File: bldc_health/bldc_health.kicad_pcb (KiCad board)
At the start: 2 copper layers, 30.1 x 30.1 mm, 51 parts, among them J1 USB-C, J2 UART, J6 SWD, SW1 BOOT_SW, SW2 RESET_SW, U1 STM32G491, U2 ASM330, U3 ICM40609, U4 AMS1117-3.3, Y1 HSE 8MHz

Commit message: changes to pins
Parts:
- C1, C10, C11, C12, C13, C14, C16, C17, C18, C19, C2, C20, C3, C4, C5, C6, C7, C8, C9: footprint C_0603_1608Metric_Pad1.08x0.95mm_HandSolder -> Capacitor_SMD:C_0603_1608Metric_Pad1.08x0.95mm_HandSolder
- C15: value 10n -> 10N; footprint C_0603_1608Metric_Pad1.08x0.95mm_HandSolder -> Capacitor_SMD:C_0603_1608Metric_Pad1.08x0.95mm_HandSolder
- D2: footprint LED_0805_2012Metric_Pad1.15x1.40mm_HandSolder -> LED_SMD:LED_0805_2012Metric_Pad1.15x1.40mm_HandSolder
- D4: value DEBUG LED -> debug_led; footprint LED_0805_2012Metric_Pad1.15x1.40mm_HandSolder -> LED_SMD:LED_0805_2012Metric_Pad1.15x1.40mm_HandSolder
- F2: value Polyfuse -> Polyfuse_Small; footprint Fuse_0603_1608Metric_Pad1.05x0.95mm_HandSolder -> Fuse:Fuse_0603_1608Metric_Pad1.05x0.95mm_HandSolder
- FB2: footprint L_0603_1608Metric_Pad1.05x0.95mm_HandSolder -> Inductor_SMD:L_0603_1608Metric_Pad1.05x0.95mm_HandSolder
- J1: value USB-C -> USB_C_Receptacle_USB2.0_14P
- J6: value SWD -> SERIAL; footprint PinHeader_1x05_P2.54mm_Vertical -> Connector_PinHeader_2.54mm:PinHeader_1x05_P2.54mm_Vertical
- JP6: value ADDR_ICM -> ICM_SJ
- JP7: value ADDR_ASM -> ICM_SJ
- R1, R10, R12, R2, R3, R4, R5, R6, R7, R8, R9: footprint R_0603_1608Metric_Pad0.98x0.95mm_HandSolder -> Resistor_SMD:R_0603_1608Metric_Pad0.98x0.95mm_HandSolder
- SW1: value BOOT_SW -> SW_SPDT; footprint SW_Slide-03_Wuerth-WS-SLTV_10x2.5x6.4_P2.54mm -> Button_Switch_THT:SW_Slide-03_Wuerth-WS-SLTV_10x2.5x6.4_P2.54mm
- SW2: value RESET_SW -> Reset
- U1: value STM32G491 -> ~; footprint QFN-48-1EP_7x7mm_P0.5mm_EP5.6x5.6mm -> EasyEDA_Lib:UFQFPN-48_L7.0-W7.0-P0.50-TL-EP5.6
- U2: value ASM330 -> ~; footprint LGA-14_3x2.5mm_P0.5mm_LayoutBorder3x4y -> EasyEDA_Lib:LGA-14_L3.0-W2.5-P0.50-TL
- U3: value ICM40609 -> ~; footprint InvenSense_QFN-24_3x3mm_P0.4mm -> EasyEDA_Lib:LGA-24_L3.0-W3.0-P0.40-TL
- U4: footprint SOT-223-3_TabPin2 -> Package_TO_SOT_SMD:SOT-223-3_TabPin2
- Y1: value HSE 8MHz -> Crystal; footprint Crystal_SMD_HC49-SD -> Crystal:Crystal_SMD_HC49-SD
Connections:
- J1 pad A1: GND -> (no net)
- J1 pad A4: /VBUS -> (no net)
- J1 pad SH: GND -> (no net)
- U1 pad 30: /SCL_ASM -> /SDA_ASM
- U1 pad 31: unconnected-(U1-PA9-Pad31) -> /SCL_ASM
- U1 pad 40: /SDA_ASM -> unconnected-(U1-PC11-Pad40)

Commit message: Update PCB layout and schematic
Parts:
- removed MH1, MH3, MH4: MountingHole_M3, MountingHole_3.2mm_M3_Pad_Via
- added MH2: MountingHole_M3, MountingHole_3.2mm_M3_Pad_Via, B.Cu at (102.9, 104.5)
- added MH5: MountingHole_M3, MountingHole_3.2mm_M3_Pad_Via, B.Cu at (126.2, 104.5)
- added MH6: MountingHole_M3, MountingHole_3.2mm_M3_Pad_Via, B.Cu at (102.9, 127.8)
- moved MH7 24.5 mm to (126.2, 127.8)
- moved FB2 7.17 mm to (130.1, 121.3), turned to -90 degrees
- moved C16 5.64 mm to (109.7, 128.7)
- moved C4 4.63 mm to (122.8, 131.7), turned to -90 degrees
- moved C17 4.13 mm to (117.2, 126.5), turned to 180 degrees
- moved Y1 3.56 mm to (113.5, 130.5)
- moved C3 3.14 mm to (130.4, 125.0)
- moved C19 2.77 mm to (121.0, 125.6)
- moved C20 2.00 mm to (121.1, 128.5), turned to -90 degrees
- moved C9 1.75 mm to (127.1, 123.3)
- moved C10 0.44 mm to (114.8, 117.9)
- moved C11 0.44 mm to (115.3, 115.1)
- moved C18 0.44 mm to (103.0, 126.9)
- moved C6 0.44 mm to (114.7, 120.5)
- moved C8 0.44 mm to (127.4, 117.0)
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- renumbered MH2 to MH7
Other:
- board size 30.1 x 30.1 mm -> 35.4 x 35.3 mm

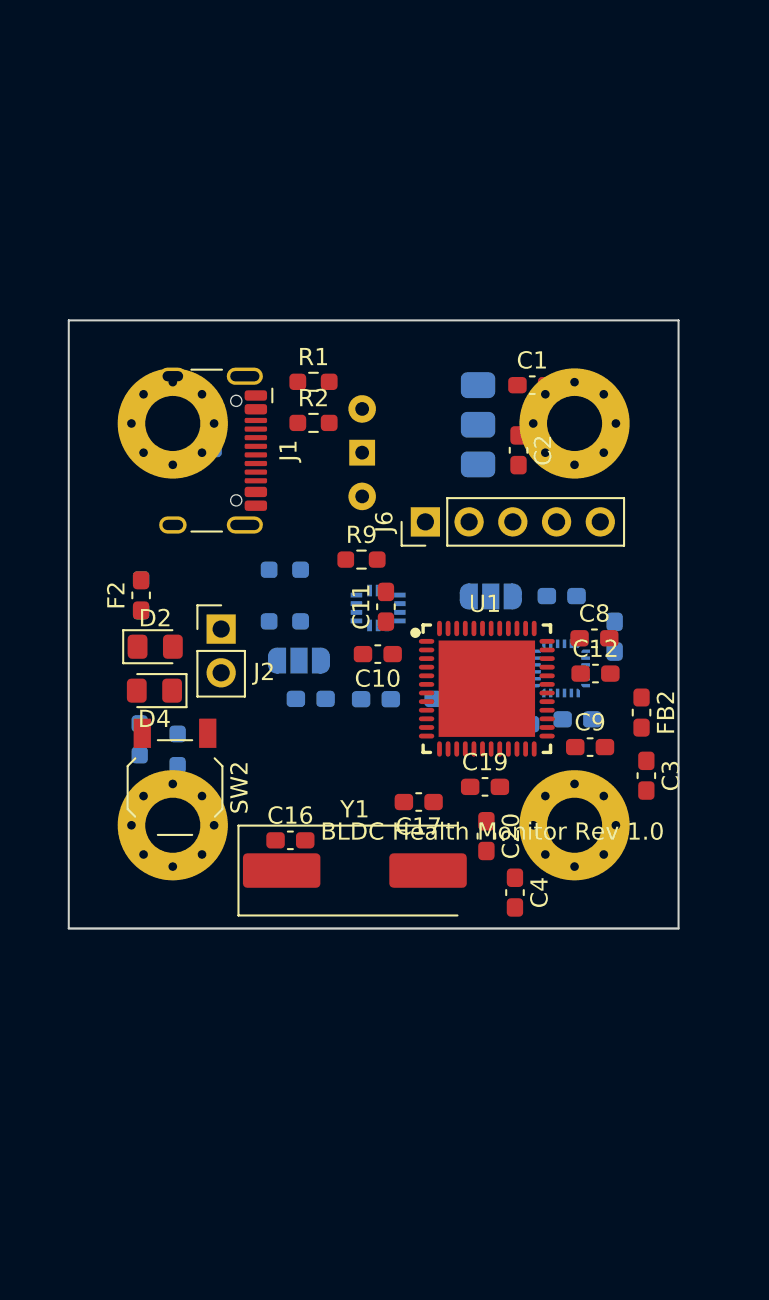
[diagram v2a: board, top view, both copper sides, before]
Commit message: Update PCB layout, footprints, and schematic
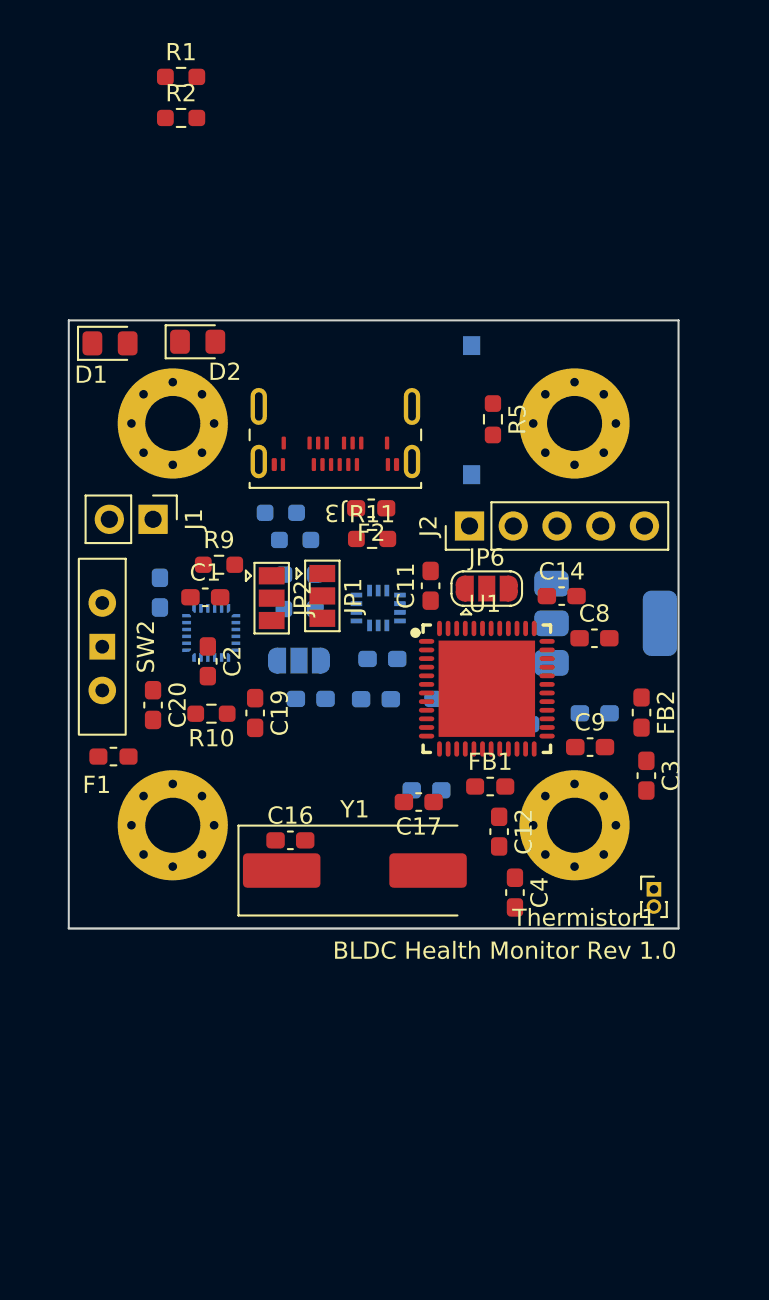
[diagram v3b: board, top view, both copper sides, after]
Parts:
- removed D4: debug_led, LED_SMD:LED_0805_2012Metric_Pad1.15x1.40mm_HandSolder
- removed J6: SERIAL, Connector_PinHeader_2.54mm:PinHeader_1x05_P2.54mm_Vertical
- added D1: 5V LED, LED_SMD:LED_0805_2012Metric_Pad1.15x1.40mm_HandSolder, F.Cu at (99.2, 99.8)
- added F1: Polyfuse_Small, Fuse:Fuse_0603_1608Metric_Pad1.05x0.95mm_HandSolder, F.Cu at (99.4, 123.8)
- added FB1: 120R, Inductor_SMD:L_0603_1608Metric_Pad1.05x0.95mm_HandSolder, F.Cu at (121.3, 125.6)
- added J3: USB_C_Receptacle_USB2.0_14P, Connector_USB:USB_C_Receptacle_Amphenol_124019772112A, F.Cu at (112.3, 103.7)
- added JP1: ICM_SJ, Jumper:SolderJumper-3_P1.3mm_Open_Pad1.0x1.5mm, F.Cu at (111.6, 114.5)
- added JP2: ICM_SJ, Jumper:SolderJumper-3_P1.3mm_Open_Pad1.0x1.5mm, F.Cu at (108.6, 114.6)
- added R11: 5k1, Resistor_SMD:R_0603_1608Metric_Pad0.98x0.95mm_HandSolder, F.Cu at (114.5, 111.2)
- added Thermistor1: 10k, Connector_PinHeader_1.00mm:PinHeader_1x02_P1.00mm_Vertical, F.Cu at (130.8, 131.6)
- C1, C2: value 10u -> 100n
- C10: value 100nF -> 100n; moved to B.Cu
- C12: value 100nF -> 10uF
- C13: value 100n -> 100nF
- C14: value 2.2u -> 100nF; moved to F.Cu
- C15: value 10N -> 100nF
- C16, C17: value 33p -> 10u
- C18: value 100nF -> 10N
- C20: value 1uF -> 2.2u
- C3: value 10uF -> 100n
- C4, C6: value 100n -> 33p
- C5: value 100n -> 10u
- C7: value 10u -> 1uF
- D2: value 5V LED -> debug_led
- J1: value USB_C_Receptacle_USB2.0_14P -> UART; footprint USB_C_Receptacle_HCTL_HC-TYPE-C-16P-01A -> Connector_PinHeader_2.54mm:PinHeader_1x02_P2.54mm_Vertical
- J2: value UART -> SERIAL; footprint PinHeader_1x02_P2.54mm_Vertical -> Connector_PinHeader_2.54mm:PinHeader_1x05_P2.54mm_Vertical
- JP6, R10: moved to F.Cu
- R1: value 5k1 -> 500
- R12: value 500 -> 5k1
- R2: value 5k1 -> 1k
- R5: value 1k5 -> 10k; moved to F.Cu
- R8: value 1k -> 1k5
- SW1: value SW_SPDT -> Reset; footprint Button_Switch_THT:SW_Slide-03_Wuerth-WS-SLTV_10x2.5x6.4_P2.54mm -> TS09-63-25-WT-160-SMT-TR:SW_TS09-63-25-WT-160-SMT-TR
- SW2: value Reset -> SW_SPDT; footprint SW_SPST_TL3342 -> Button_Switch_THT:SW_Slide-03_Wuerth-WS-SLTV_10x2.5x6.4_P2.54mm
- U3: value ~ -> AMS1117-3.3; footprint EasyEDA_Lib:LGA-24_L3.0-W3.0-P0.40-TL -> Package_TO_SOT_SMD:SOT-223-3_TabPin2
- U4: value AMS1117-3.3 -> ~; footprint Package_TO_SOT_SMD:SOT-223-3_TabPin2 -> EasyEDA_Lib:LGA-24_L3.0-W3.0-P0.40-TL
- moved C1 22.6 mm to (104.8, 114.6)
- moved U4 22.2 mm to (105.1, 116.7)
- moved C2 21.8 mm to (104.9, 118.3)
- moved C20 20.8 mm to (101.7, 120.8)
- moved R1 19.3 mm to (103.4, 84.4)
- moved R2 19.3 mm to (103.4, 86.8)
- moved D2 17.9 mm to (104.3, 99.8)
- moved R5 17.2 mm to (121.5, 104.2), turned to -90 degrees
- moved J2 15.6 mm to (120.1, 110.5), turned to 90 degrees
- moved R8 15.5 mm to (109.2, 109.7), turned to 180 degrees
- moved F2 14.3 mm to (114.4, 109.4), turned to 180 degrees
- moved C19 14.0 mm to (107.7, 121.3), turned to -90 degrees
- moved C15 13.5 mm to (115.0, 118.2), turned to 0 degrees
- moved C18 12.6 mm to (102.1, 114.3), turned to -90 degrees
- moved C12 10.8 mm to (121.8, 128.2), turned to -90 degrees
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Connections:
- C1 pad 1: /VBUS -> /VDDA
- C10 pad 1: /VDD_STM -> /VDDA
- C13 pad 1: /VDD -> /VDD_STM
- C14 pad 1: /VDD -> /VDD_STM
- C15 pad 1: GND -> /VDD_STM
- C15 pad 2: /VDD -> GND
- C16 pad 1: /HSE_IN -> /VBUS
- C17 pad 1: /HSE_OUT -> /VDD
- C18 pad 2: /Reset -> /VDD
- C19 pad 1: /VDDA -> /VDD
- C20 pad 1: /VDDA -> /VDD
- C3 pad 1: /VDD_STM -> /VDD
- C4 pad 1: /VDDA -> /HSE_IN
- C6 pad 1: /VDD -> /HSE_OUT
- C7 pad 1: /VDD -> /VDDA
- C9 pad 1: /VDD_STM -> GND
- C9 pad 2: GND -> /Reset
- D2 pad 1: Net-(D2-K) -> GND
- D2 pad 2: /VBUS -> Net-(D2-A)
- J2 pad 1: /PA2_TX -> /VDD
- J2 pad 2: /PA3_RX -> /SWDIO
- R1 pad 1: Net-(J1-CC1) -> Net-(D1-K)
- R10 pad 1: /Reset -> /SCL_ICM
- R12 pad 1: Net-(D2-K) -> Net-(J3-CC2)
- R2 pad 1: Net-(J1-CC2) -> Net-(D2-A)
- R2 pad 2: GND -> /PB2
- R5 pad 1: /USB_D+ -> /Reset
- R6 pad 1: /VDD -> /VDDA
- R6 pad 2: /SDA_ICM -> /PA0
- R7 pad 1: /SCL_ICM -> Net-(SW2-B)
- R7 pad 2: /VDD -> /Boot0
- R8 pad 1: Net-(D4-A) -> /USB_D+
- R8 pad 2: /PB2 -> /VDD
- R9 pad 1: Net-(SW1-B) -> /VDD
- R9 pad 2: /Boot0 -> /SDA_ICM
- SW1 pad 1: GND -> /Reset
- SW1 pad 2: Net-(SW1-B) -> GND
- SW2 pad 1: /Reset -> GND
- SW2 pad 2: GND -> Net-(SW2-B)
- U1 pad 8: unconnected-(U1-PA0-Pad8) -> /PA0
- U2 pad 1: Net-(JP7-C) -> Net-(JP1-C)
- U3 pad 1: unconnected-(U3-NC-Pad1) -> GND
- U3 pad 2: unconnected-(U3-NC-Pad2) -> /VDD
- U3 pad 3: unconnected-(U3-NC-Pad3) -> /VBUS
- U4 pad 1: GND -> unconnected-(U4-NC-Pad1)
- U4 pad 2: /VDD -> unconnected-(U4-NC-Pad2)
- U4 pad 3: /VBUS -> unconnected-(U4-NC-Pad3)

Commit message: Back up current PCB and design settings before routing cleanup
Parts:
- R2: moved to B.Cu
- moved R2 39.0 mm to (113.6, 124.4), turned to 90 degrees
- moved D2 26.0 mm to (110.2, 125.0)
- moved R1 20.8 mm to (97.9, 104.4), turned to -90 degrees
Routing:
- net /VDD: track 0.00 -> 133.5 mm, vias 0 -> 16
- net /VDD_STM: track 0.00 -> 115.8 mm, vias 0 -> 14
- net /INT1: track 0.00 -> 87.8 mm, vias 0 -> 7
- net /VBUS: track 0.00 -> 69.4 mm, vias 0 -> 3
- net /VDDA: track 0.00 -> 60.2 mm, vias 0 -> 2
- net /PA3_RX: track 0.00 -> 48.8 mm, vias 0 -> 4
- net Net-(SW2-B): track 0.00 -> 46.4 mm, vias 0 -> 1
- net /Reset: track 0.00 -> 44.6 mm, vias 0 -> 1
- net /PB0_INT1_ICM: track 0.00 -> 32.5 mm, vias 0 -> 4
- net /PA0: track 0.00 -> 17.5 mm
- net /SWDIO: track 0.00 -> 15.0 mm
- net /PB2: track 0.00 -> 13.5 mm, vias 0 -> 2
- net /SWO: track 0.00 -> 10.8 mm, vias 0 -> 1
- net Net-(J3-CC2): track 0.00 -> 8.60 mm, vias 0 -> 1
- net /HSE_OUT: track 0.00 -> 8.20 mm, vias 0 -> 2
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- added copper zone on B.Cu, net GND
- added copper zone on F.Cu, net GND

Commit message: Preserve current open KiCad routing in pre-edit backup
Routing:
- net /PA2_TX: track 5.03 -> 28.6 mm, vias 0 -> 4
- net /HSE_IN: track 0.00 -> 17.7 mm, vias 0 -> 2
- net /Boot0: track 0.00 -> 6.70 mm, vias 0 -> 1
- net /PB2: track 13.5 -> 16.8 mm, vias 2 -> 3
- net /HSE_OUT: track 8.20 -> 4.98 mm, vias 2 -> 1
- net Net-(SW2-B): track 46.4 -> 45.8 mm
- net /FSYNC: track 0.00 -> 0.40 mm, vias 0 -> 2
- net /INT2: vias 1 -> 2

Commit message: Improve PCB placement and routing; retain three unresolved connections
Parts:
- moved C8 2.33 mm to (129.7, 117.0)
- moved C16 1.90 mm to (109.7, 126.8)
- moved U3 0.32 mm to (128.1, 115.8), turned to -90 degrees
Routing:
- net GND: track 0.00 -> 126.8 mm, vias 0 -> 15
- net /INT1: track 87.8 -> 19.9 mm, vias 7 -> 1
- net /USB_D+: track 0.00 -> 42.4 mm, vias 0 -> 4
- net /USB_D-: track 0.00 -> 33.8 mm, vias 0 -> 2
- net /SDA_ICM: track 0.00 -> 31.5 mm, vias 0 -> 5
- net /SCL_ASM: track 0.00 -> 30.0 mm, vias 0 -> 3
- net /FSYNC: track 0.40 -> 24.4 mm, vias 2 -> 5
- net /PA0: track 17.5 -> 40.1 mm, vias 0 -> 3
- net /SDA_ASM: track 0.00 -> 21.0 mm, vias 0 -> 1
- net /PA3_RX: track 48.8 -> 30.4 mm, vias 4 -> 0
- net /VBUS: track 69.4 -> 86.6 mm, vias 3 -> 4
- net /HSE_OUT: track 4.98 -> 21.3 mm, vias 1 -> 2
- net /HSE_IN: track 17.7 -> 32.9 mm, vias 2 -> 4
- net /PB0_INT1_ICM: track 32.5 -> 20.0 mm, vias 4 -> 1
- net /INT2: track 0.00 -> 11.2 mm, vias 2 -> 1
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
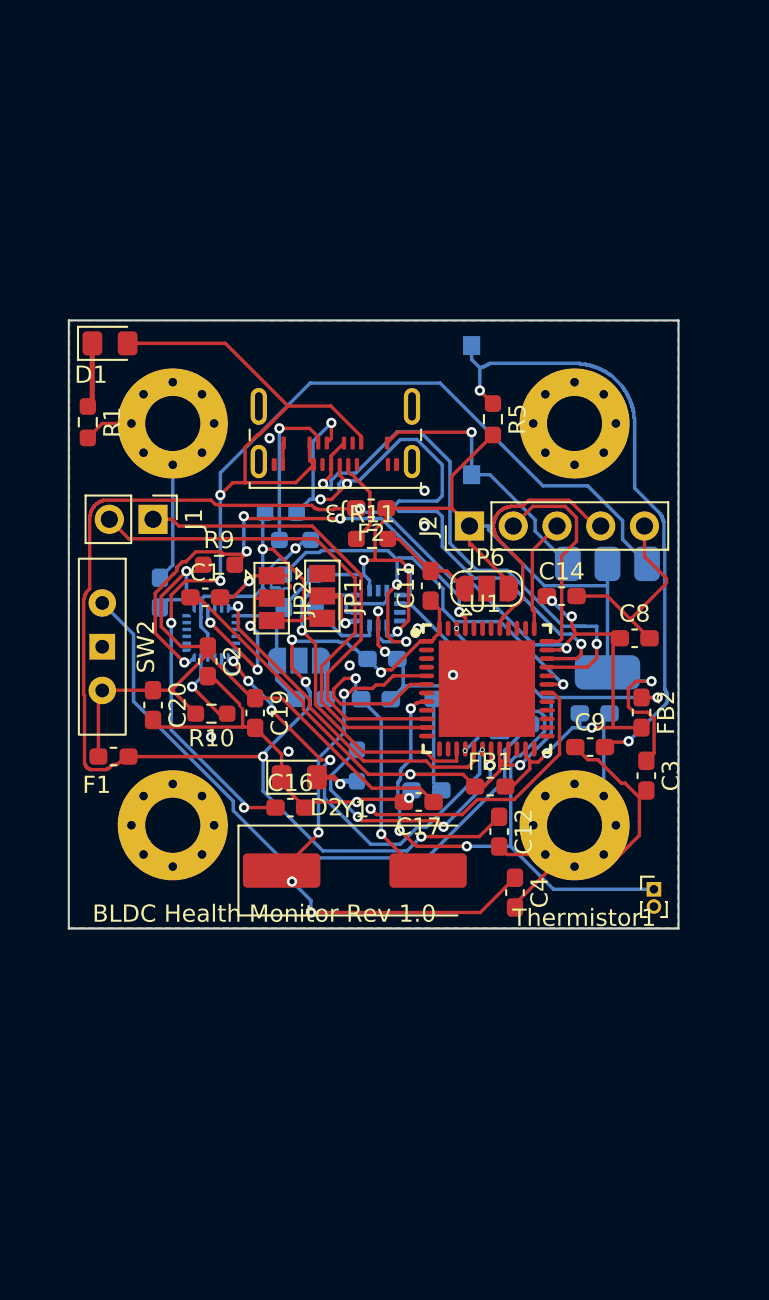
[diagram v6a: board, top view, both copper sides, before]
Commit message: Preserve user PCB and ground-zone edits before review fixes
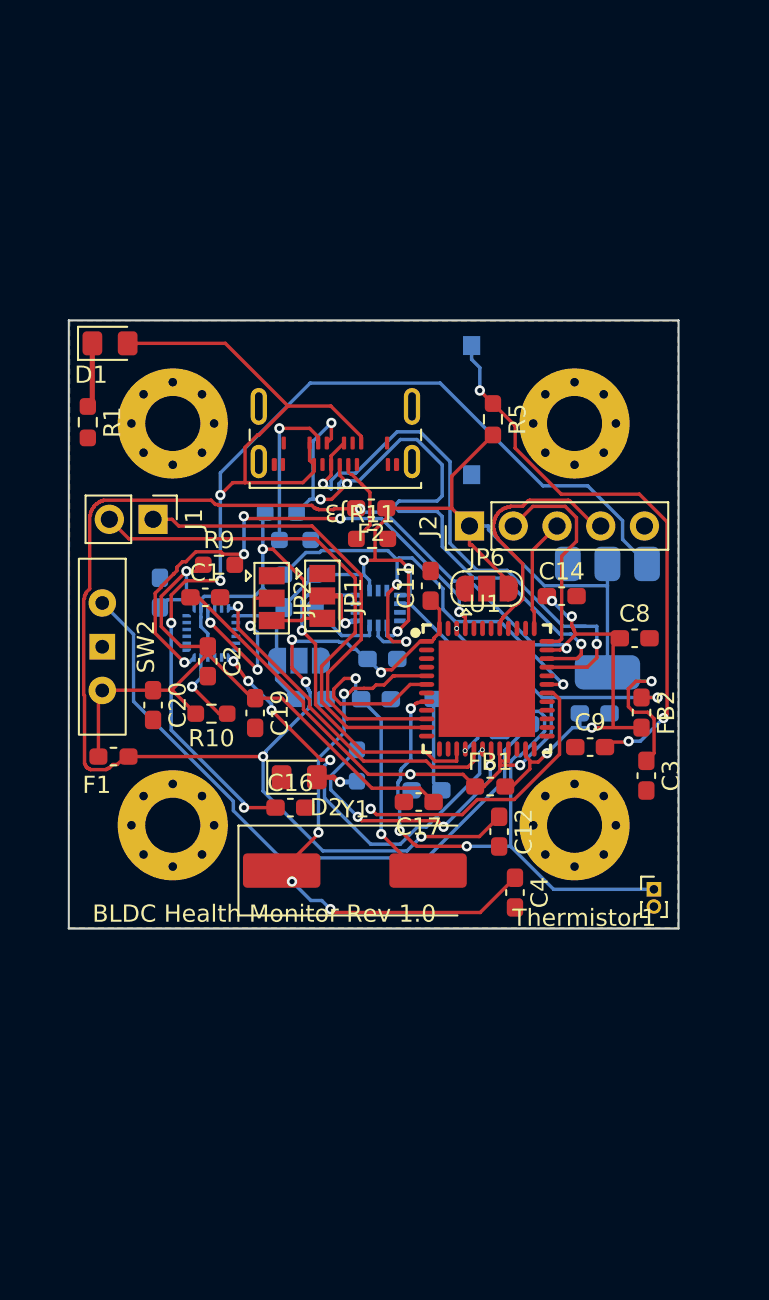
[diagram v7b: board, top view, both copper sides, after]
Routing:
- net GND: track 126.8 -> 0.00 mm, vias 15 -> 0
- net /Reset: track 36.2 -> 32.5 mm, vias 2 -> 3

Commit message: Apply verified PCB review fixes before USB footprint replacement
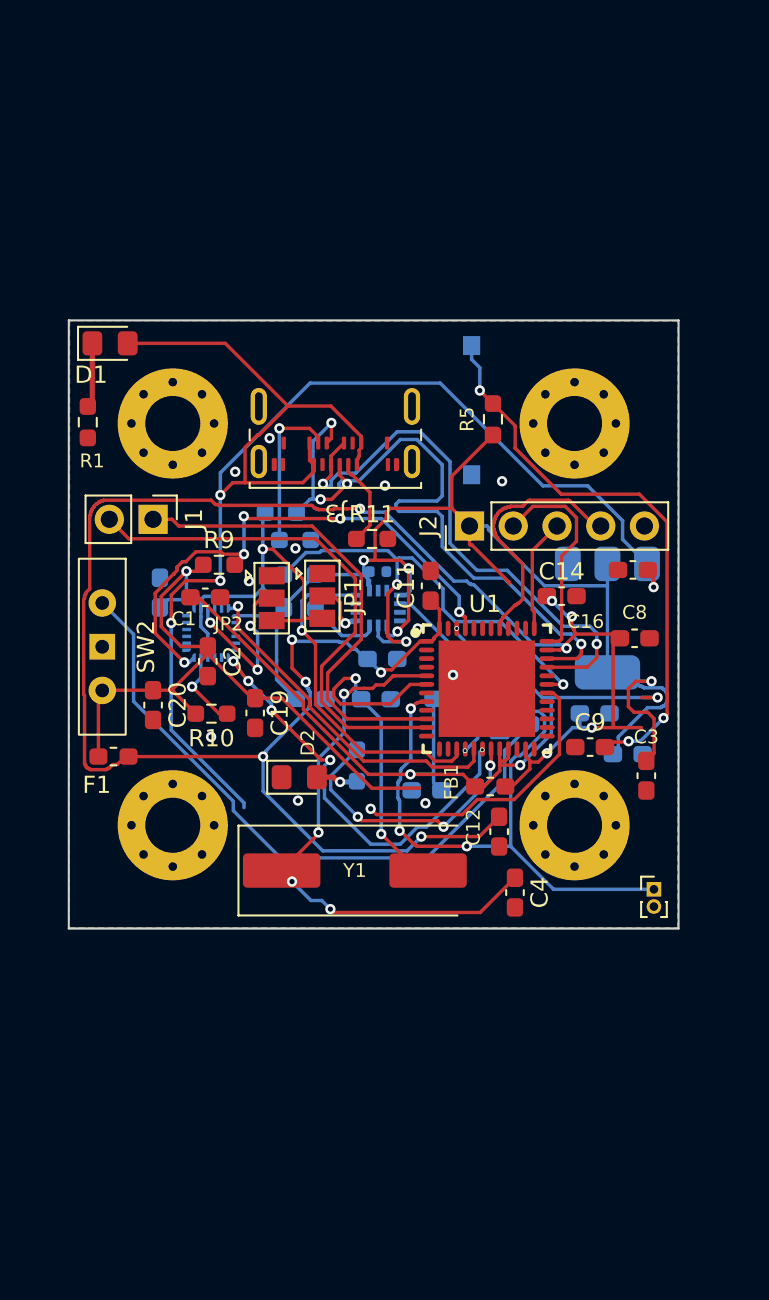
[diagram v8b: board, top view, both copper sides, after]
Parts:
- removed F2: Polyfuse_Small, Fuse:Fuse_0603_1608Metric_Pad1.05x0.95mm_HandSolder
- removed FB2: 120R, Inductor_SMD:L_0603_1608Metric_Pad1.05x0.95mm_HandSolder
- removed JP6, JP7: ICM_SJ, SolderJumper-3_P1.3mm_Open_RoundedPad1.0x1.5mm
- added C21: 100nF, Capacitor_SMD:C_0402_1005Metric, B.Cu at (114.8, 113.1)
- C17: moved to B.Cu
- Y1: value Crystal -> 8MHz CL20pF
- moved C16 24.2 mm to (129.6, 113.0), turned to 180 degrees
- moved C17 12.5 mm to (129.3, 123.7), turned to 0 degrees
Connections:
- J3 pad A1: (no net) -> GND
- J3 pad A4: (no net) -> /VBUS
- J3 pad SH: (no net) -> GND
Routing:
- net /VDD: track 134.3 -> 139.6 mm
- net /VDD_STM: track 116.2 -> 117.0 mm
- net GND: vias 0 -> 11
